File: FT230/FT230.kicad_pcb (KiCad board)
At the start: 2 copper layers, 20.5 x 10.4 mm, 22 parts, among them J1 SolderJumper_2_Open, J1 USB_B_Micro, J2 Conn_01x04, J3 Conn_01x02, J4 Conn_01x02, U1 FT230XQ

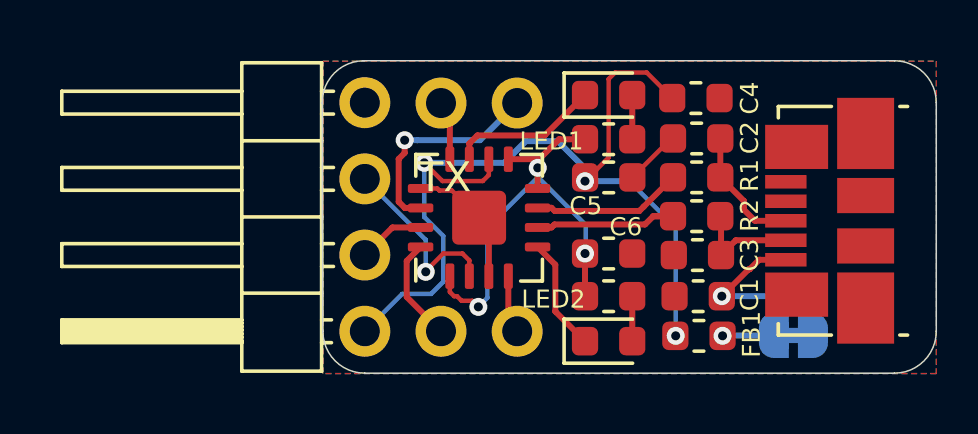
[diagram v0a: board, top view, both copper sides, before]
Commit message: Silkscreens Updated
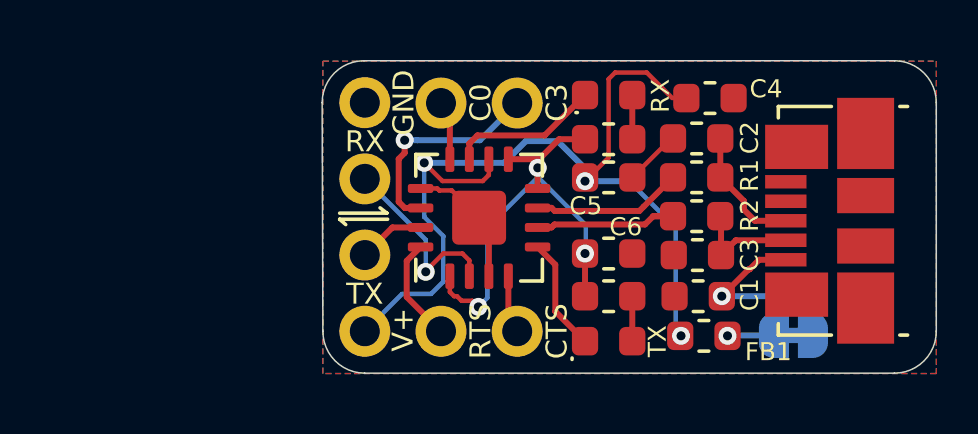
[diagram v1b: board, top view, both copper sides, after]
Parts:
- J2: footprint Connector_PinHeader_2.54mm:PinHeader_1x04_P2.54mm_Horizontal -> Connector_PinHeader_2.54mm:PinHeader_1x04_P2.54mm_Vertical; moved to B.Cu
- moved C4 0.47 mm to (207.6, 68.1)
- moved FB1 0.17 mm to (207.4, 76.0)
- turned J2 to 0 degrees
- renumbered LED1 to RX, LED2 to TX

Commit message: Silkscreen Updates
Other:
- board text added: "FT230X USB-UART"
- board text removed: "UART to USB"
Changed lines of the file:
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@@
     (effects (font (size 0.85 0.7) (thickness 0.13)) (justify mirror))
   )
-  (gr_text "UART to USB" (at 207.2005 72.009 90) (layer B.SilkS)
-    (effects (font (size 0.8 0.8) (thickness 0.15)) (justify mirror))
+  (gr_text "FT230X USB-UART" (at 207.2005 72.009 90) (layer B.SilkS)
+    (effects (font (size 0.7 0.7) (thickness 0.12)) (justify mirror))
   )
   (gr_arc (start 213.741 75.8698) (end 213.741 77.2668) (angle -90) (layer Edge.Cuts) (width 0.05))

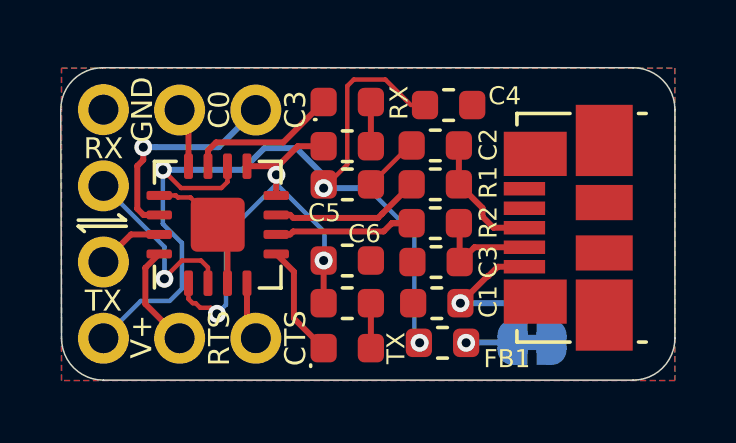
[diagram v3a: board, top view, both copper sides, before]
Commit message: Power LED Added
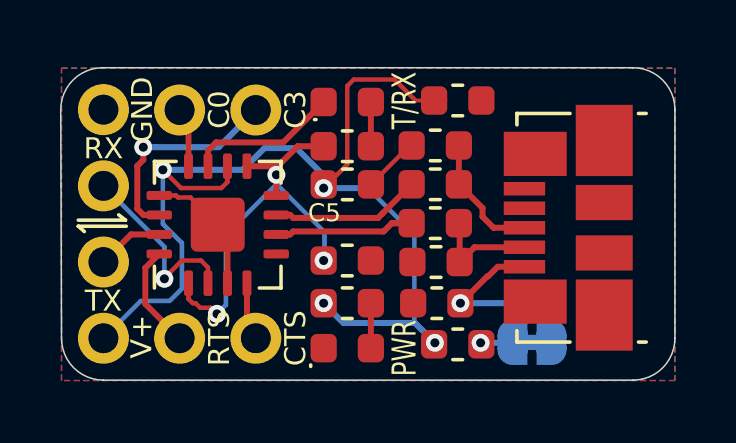
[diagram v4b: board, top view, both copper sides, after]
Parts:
- PWR: renamed from TX; value TX -> PWR
- R3: value R_US -> 270E
- R4: value R_US -> 1K
- moved FB1 0.51 mm to (207.9, 76.1)
- moved C4 0.34 mm to (207.9, 67.9)
- renumbered J1 to JP1, RX to T/RX
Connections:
- net Net-(C1-Pad1) renamed /VUSB
- C4 pad 1: /5V -> /VCC
- C5 pad 1: /5V -> /VCC
- C6 pad 1: Net-(C6-Pad1) -> /3.3V
- FB1 pad 1: /5V -> /VCC
- J2 pad 1: /5V -> /VCC
- PWR pad 1: Net-(LED2-Pad1) -> GND
- R3 pad 1: Net-(C6-Pad1) -> /3.3V
- R4 pad 1: Net-(C6-Pad1) -> /VCC
- U1 pad 1: Net-(C6-Pad1) -> /3.3V
- U1 pad 10: /5V -> /VCC
- U1 pad 5: Net-(LED2-Pad1) -> Net-(U1-Pad5)
- U1 pad 8: Net-(C6-Pad1) -> /3.3V
- U1 pad 9: Net-(C6-Pad1) -> /3.3V
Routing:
- net /VCC: track 0.00 -> 35.7 mm, vias 0 -> 4
- net /5V: track 31.5 -> 0.00 mm, vias 3 -> 0
- net Net-(C6-Pad1): track 15.5 -> 0.00 mm, vias 3 -> 0
- net /3.3V: track 0.00 -> 14.1 mm, vias 0 -> 3
- net Net-(LED2-Pad1): track 3.79 -> 0.00 mm
- net Net-(FB1-Pad2): track 1.75 -> 1.07 mm

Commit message: Silkscreen Edits
Dimensions moved to Drawings Layer
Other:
- rule pad_to_mask_clearance: 0.051 -> 0
- rule solder_mask_min_width: 0.25 -> 0.1

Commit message: Page Settings Updated
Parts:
- moved C1 140.7 mm to (69.5, 45.9)
- moved C2 140.7 mm to (69.5, 40.6)
- moved C3 140.7 mm to (69.5, 44.5)
- moved C4 140.7 mm to (70.2, 39.1)
- moved C5 140.7 mm to (66.6, 41.9)
- moved C6 140.7 mm to (66.5, 44.5)
- moved FB1 140.7 mm to (70.2, 47.2)
- moved G*** 140.7 mm to (67.5, 43.2)
- moved J1 140.7 mm to (73.9, 43.4)
- moved J2 140.7 mm to (58.4, 47.0)
- moved JP1 140.7 mm to (72.7, 47.2)
- moved PWR 140.7 mm to (66.5, 47.4)
- moved R1 140.7 mm to (69.5, 41.9)
- moved R2 140.7 mm to (69.5, 43.2)
- moved R3 140.7 mm to (66.5, 40.6)
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
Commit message: Part Numbers Added
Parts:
- C5: footprint Capacitor_SMD:C_0603_1608Metric -> Capacitor_SMD:C_0805_2012Metric
- moved REF** 1.46 mm to (72.9, 41.7)
- moved J2 0.64 mm to (57.8, 47.0)
- moved R3 0.36 mm to (66.8, 40.4)
- moved TX/RX 0.28 mm to (66.8, 39.1)
- moved PWR 0.25 mm to (66.8, 47.4)
- moved R4 0.25 mm to (66.8, 45.9)
- moved C2 0.25 mm to (69.7, 40.6)
- moved R1 0.25 mm to (69.7, 41.9)
- moved R2 0.24 mm to (69.7, 43.2)
- moved C3 0.22 mm to (69.7, 44.5)
- moved C1 0.19 mm to (69.7, 45.8)
- moved J3 0.19 mm to (60.8, 47.0)
- moved J4 0.19 mm to (60.8, 39.4)
- renumbered T/RX to TX/RX
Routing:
- net /VCC: track 35.7 -> 38.6 mm
- net GND: track 6.33 -> 4.50 mm
- net Net-(FB1-Pad2): track 1.07 -> 2.90 mm
- net /uD-: track 5.57 -> 4.91 mm
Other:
- board size 20.5 x 10.4 mm -> 21.1 x 10.4 mm
- board text added: "VCC"
- board text added: "VUSB"
